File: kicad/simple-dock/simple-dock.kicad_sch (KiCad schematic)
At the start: 0 parts

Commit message: more kicad
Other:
- added sheet audio (audio.kicad_sch)
- added sheet hdmi (hdmi.kicad_sch)
- added sheet jtag_debug (jtag_debug.kicad_sch)
- added sheet sdcard (sdcard.kicad_sch)
- sheet SOM_FPGA ports: added MODE{0 1 2}, {DBUG}, {DVI}, {I2S}, {JTAG}, {SDIO}; removed none

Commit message: more kicad
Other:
- added sheet sdram (sdram.kicad_sch)
- sheet SOM_FPGA ports: added {SDRAM}; removed none
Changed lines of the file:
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@@
+	(bus
+		(pts
+			(xy 86.36 80.01) (xy 92.71 80.01)
+		)
+		(stroke
+			(width 0)
+			(type default)
+		)
+	)
 	(bus
 		(pts
@@
 			)
 		)
+		(pin "{SDRAM}" bidirectional
+			(at 92.71 80.01 180)
+			(effects
+				(font
+					(size 1.27 1.27)
+				)
+				(justify left)
+			)
+		)
 		(instances
 			(project "simple-dock"
@@
 				)
 			)
+		)
+	)
+	(sheet
+		(at 63.5 76.2)
+		(size 22.86 6.35)
+		(exclude_from_sim no)
+		(in_bom yes)
+		(on_board yes)
+		(dnp no)
+		(fields_autoplaced yes)
+		(stroke
+			(width 0.1524)
+			(type solid)
+		)
+		(fill
+			(color 0 0 0 0.0000)
+		)
+		(property "Sheetname" "sdram"
+			(at 63.5 75.4884 0)
+			(effects
+				(font
+					(size 1.27 1.27)
+				)
+				(justify left bottom)
+			)
+		)
+		(property "Sheetfile" "sdram.kicad_sch"
+			(at 63.5 83.1346 0)
+			(effects
+				(font
+					(size 1.27 1.27)
+				)
+				(justify left top)
+			)
+		)
+		(pin "{SDRAM}" bidirectional
+			(at 86.36 80.01 0)
+			(effects
+				(font
+					(size 1.27 1.27)
+				)
+				(justify right)
+			)
+		)
+		(instances
+			(project "simple-dock"
+				(path "/611ec8e2-0d16-4d96-a4bc-b28ea3447e62"
+					(page "7")
+				)
+			)

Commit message: more kicad
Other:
- added sheet USB (USB.kicad_sch)
- sheet SOM_FPGA ports: added {USBA1}, {USBA2}; removed none
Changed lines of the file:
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@@
 	(sheet
 		(at 92.71 20.32)
-		(size 40.64 73.66)
+		(size 40.64 86.36)
 		(exclude_from_sim no)
 		(in_bom yes)
@@
 		)
 		(property "Sheetfile" "SOM_FPGA.kicad_sch"
-			(at 92.71 94.5646 0)
+			(at 92.71 107.2646 0)
 			(effects
 				(font
@@
 			)
 		)
+		(pin "{USBA1}" bidirectional
+			(at 92.71 88.9 180)
+			(effects
+				(font
+					(size 1.27 1.27)
+				)
+				(justify left)
+			)
+		)
+		(pin "{USBA2}" bidirectional
+			(at 92.71 91.44 180)
+			(effects
+				(font
+					(size 1.27 1.27)
+				)
+				(justify left)
+			)
+		)
 		(instances
 			(project "simple-dock"
@@
 				)
 			)
+		)
+	)
+	(sheet
+		(at 63.5 87.63)
+		(size 22.86 6.35)
+		(exclude_from_sim no)
+		(in_bom yes)
+		(on_board yes)
+		(dnp no)
+		(fields_autoplaced yes)
+		(stroke
+			(width 0.1524)
+			(type solid)
+		)
+		(fill
+			(color 0 0 0 0.0000)
+		)
+		(property "Sheetname" "USB"
+			(at 63.5 86.9184 0)
+			(effects
+				(font
+					(size 1.27 1.27)
+				)
+				(justify left bottom)
+			)
+		)
+		(property "Sheetfile" "USB.kicad_sch"
+			(at 63.5 94.5646 0)
+			(effects
+				(font
+					(size 1.27 1.27)
+				)
+				(justify left top)
+			)
+		)
+		(instances
+			(project "simple-dock"
+				(path "/611ec8e2-0d16-4d96-a4bc-b28ea3447e62"
+					(page "8")
+				)
+			)

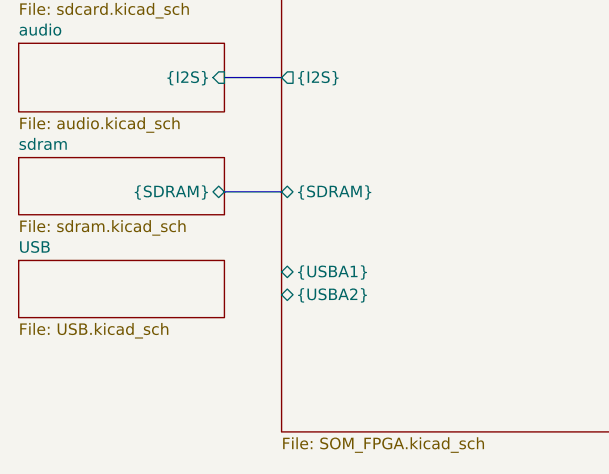
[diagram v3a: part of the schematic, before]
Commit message: kicad add usb
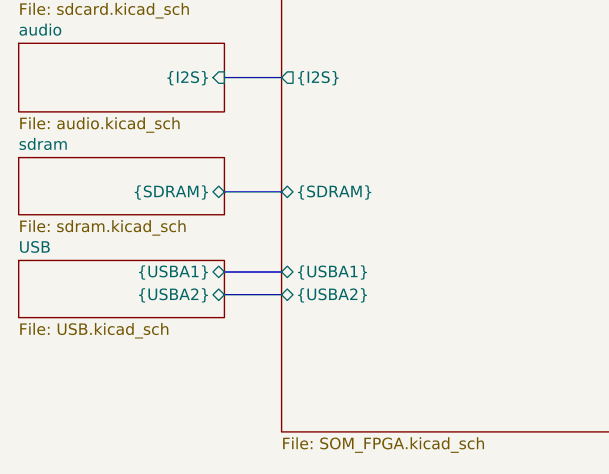
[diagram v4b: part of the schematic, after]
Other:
- sheet USB ports: added {USBA1}, {USBA2}; removed none
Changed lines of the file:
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@@
+	(bus
+		(pts
+			(xy 86.36 88.9) (xy 92.71 88.9)
+		)
+		(stroke
+			(width 0)
+			(type default)
+		)
+	)
 	(bus
 		(pts
 			(xy 86.36 24.13) (xy 92.71 24.13)
+		)
+		(stroke
+			(width 0)
+			(type default)
+		)
+	)
+	(bus
+		(pts
+			(xy 86.36 91.44) (xy 92.71 91.44)
 		)
 		(stroke
@@
 			)
 		)
+		(pin "{USBA1}" bidirectional
+			(at 86.36 88.9 0)
+			(effects
+				(font
+					(size 1.27 1.27)
+				)
+				(justify right)
+			)
+		)
+		(pin "{USBA2}" bidirectional
+			(at 86.36 91.44 0)
+			(effects
+				(font
+					(size 1.27 1.27)
+				)
+				(justify right)
+			)
+		)
